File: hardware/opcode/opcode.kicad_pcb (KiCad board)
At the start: 4 copper layers, 101.6 x 101.6 mm, 80 parts, among them J3 Conn_01x20, U1 74HC74, U10 74LVC1G00, U11 74HC595, U12 74LVC1G08, U13 74LVC1G32, U14 74HC595, U15 74LVC1G32, U16 74LVC1G32, U17 74LVC1G08, U18 74HC251, U19 74LVC1G32, U2 74HC595, U20 74HC597, U21 74HC597, U22 74HC597, U23 74HC597, U24 74HC597, U25 74HC597, U26 74HC597, U27 74HC597, U28 74HC597, U29 74HC597, U3 SST39SF040, U30 74HC597, U31 74HC597, U32 74HC597, U33 74HC597, U4 SST39SF040, U5 SST39SF040, U6 SST39SF040, U7 74HC595, U8 74HC595, U9 74LVC1G00

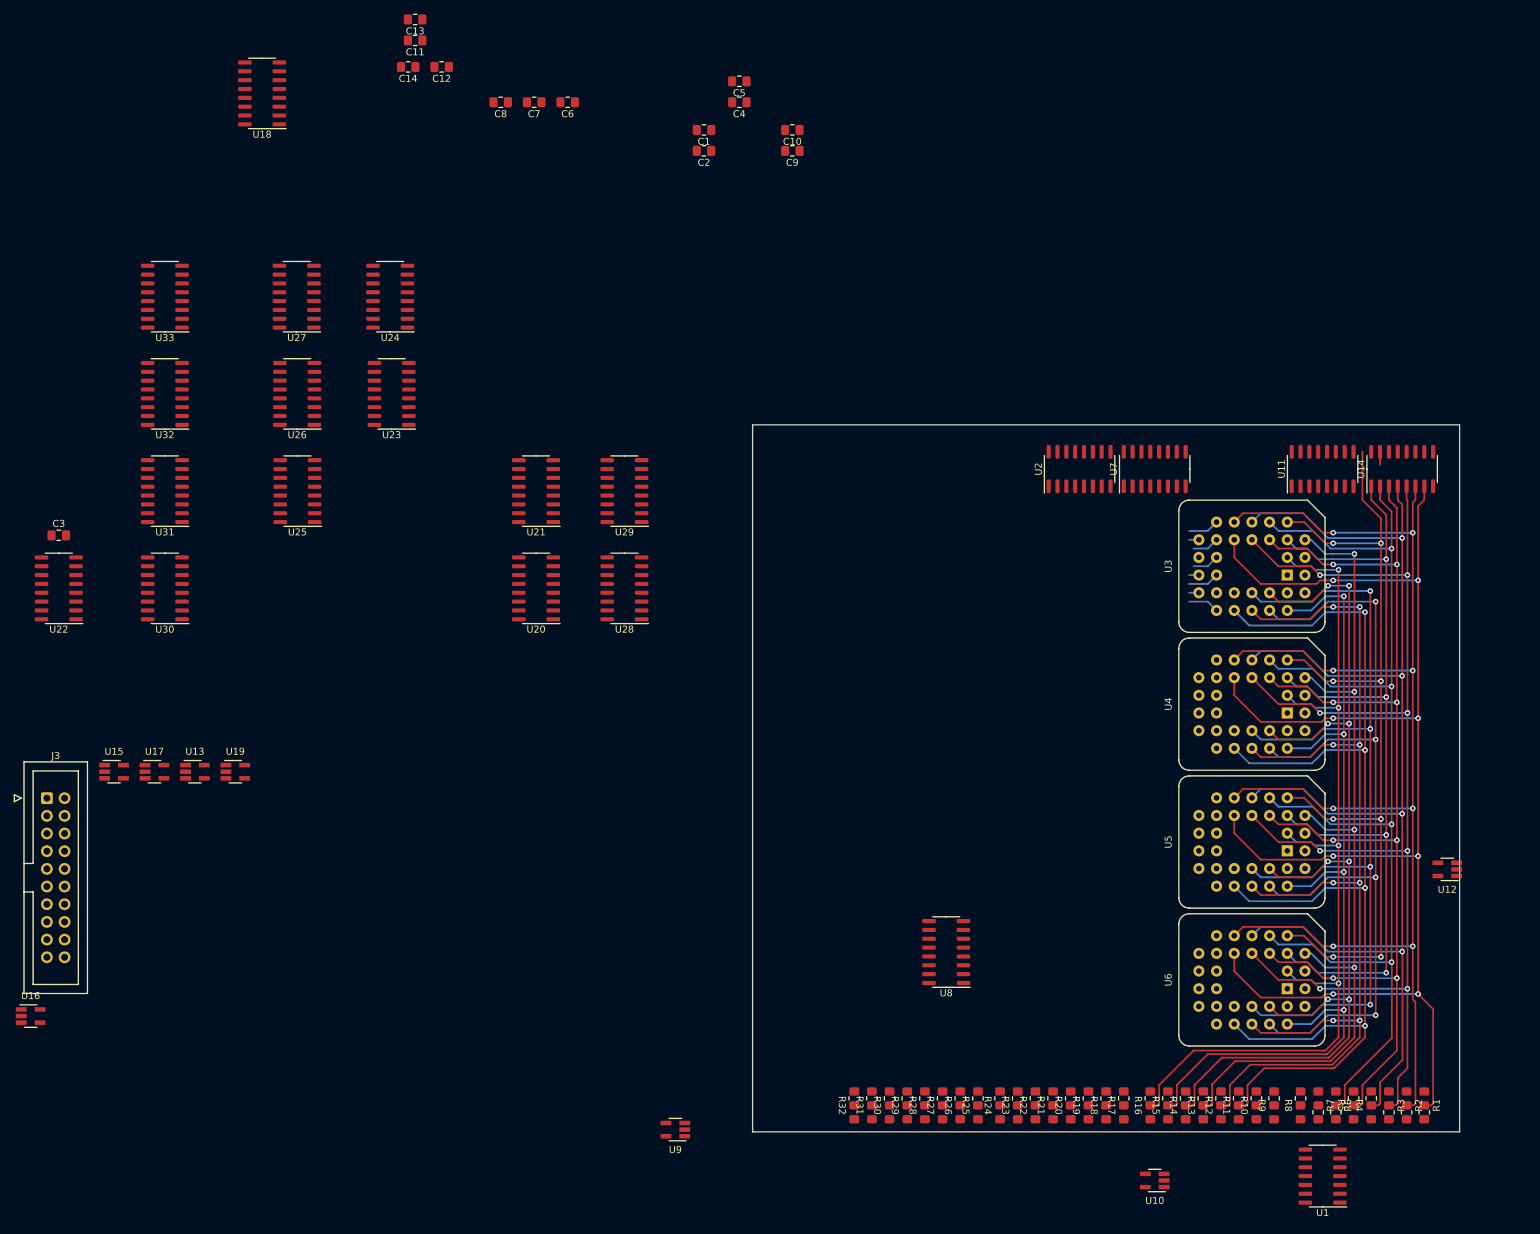
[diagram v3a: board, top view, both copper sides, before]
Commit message: Added start of adapter circuits
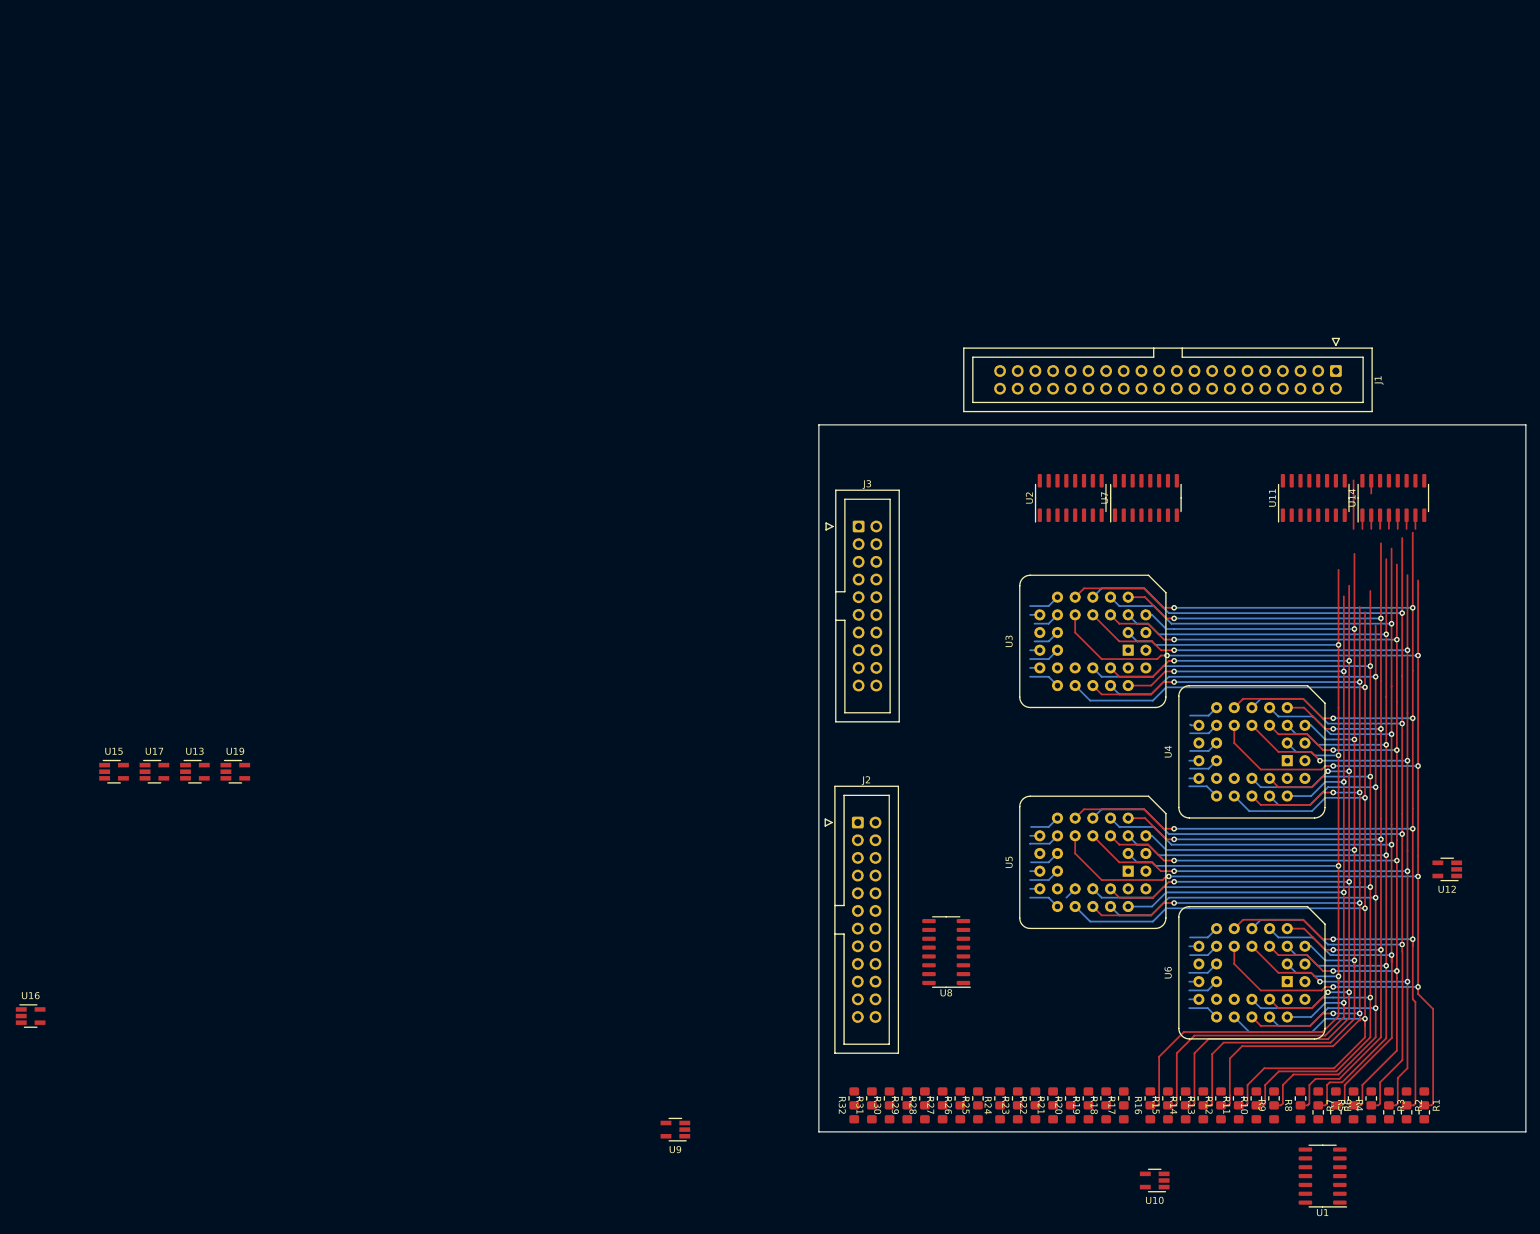
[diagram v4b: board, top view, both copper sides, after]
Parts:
- removed C1, C10, C11, C12, C13, C14, C2, C3, C4, C5, C6, C7, C8, C9: 100n, Capacitor_SMD:C_0805_2012Metric_Pad1.18x1.45mm_HandSolder
- removed U18: 74HC251, Package_SO:SOIC-16_3.9x9.9mm_P1.27mm
- removed U20, U21, U22, U23, U24, U25, U26, U27, U28, U29, U30, U31, U32, U33: 74HC597, Package_SO:SOIC-16_3.9x9.9mm_P1.27mm
- added J1: Conn_01x40, Connector_IDC:IDC-Header_2x20_P2.54mm_Vertical, F.Cu at (212.7, 38.6)
- added J2: Conn_01x24, Connector_IDC:IDC-Header_2x12_P2.54mm_Vertical, F.Cu at (144.0, 103.5)
- J3: value Conn_01x20 -> Conn_Reg_Sel
- moved J3 123.0 mm to (144.1, 61.0)
- moved U3 25.3 mm to (177.8, 77.5)
- moved U5 23.0 mm to (177.8, 109.2)
- moved U4 6.86 mm to (200.7, 93.3)
- moved U14 4.35 mm to (221.0, 56.9)
- moved U2 4.35 mm to (174.6, 56.9)
- moved U7 4.35 mm to (185.4, 56.9)
- moved U11 4.35 mm to (209.6, 56.9)
- moved U6 1.02 mm to (200.7, 125.1)
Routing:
- net /A9: track 132.1 -> 204.6 mm
- net /A7: track 134.5 -> 201.6 mm
- net /A8: track 126.7 -> 192.4 mm
- net /A6: track 132.3 -> 193.4 mm
- net /A13: track 145.6 -> 193.4 mm
- net /A12: track 128.7 -> 176.4 mm
- net /A14: track 130.1 -> 177.8 mm, vias 4 -> 5
- net /A15: track 132.3 -> 179.6 mm
- net /A10: track 166.8 -> 213.5 mm
- net /A11: track 154.4 -> 201.0 mm
- net /A1: track 199.8 -> 241.6 mm
- net /A3: track 186.1 -> 226.0 mm
- net /A5: track 169.9 -> 209.0 mm
- net /A4: track 171.7 -> 207.6 mm
- net /A2: track 188.5 -> 223.4 mm
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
